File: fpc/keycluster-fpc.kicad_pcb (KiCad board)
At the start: 2 copper layers, 15 x 13.7 mm, 2 parts

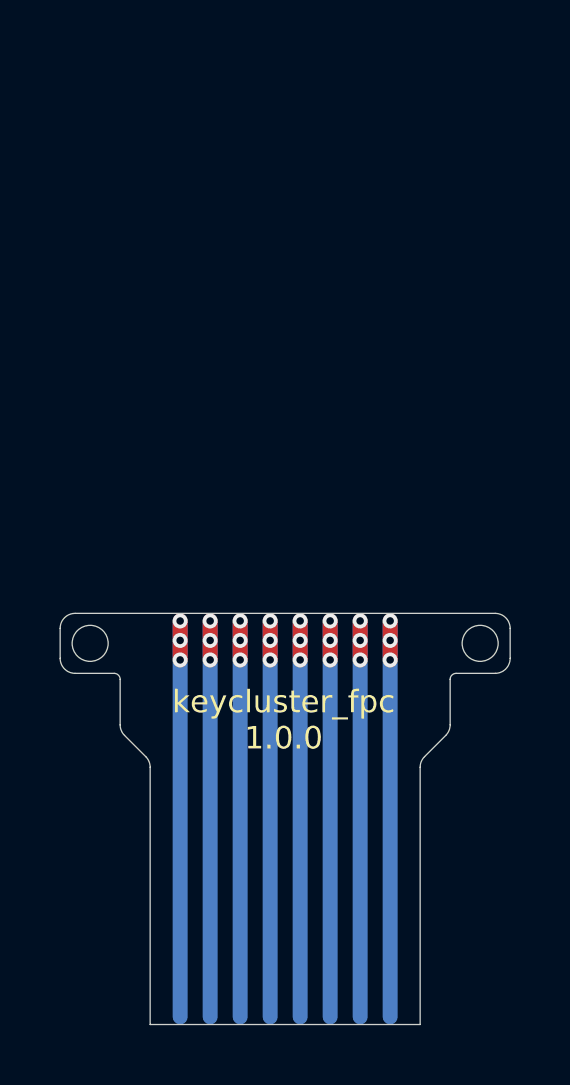
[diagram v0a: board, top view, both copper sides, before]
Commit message: Add incomplete key cluster FPC.
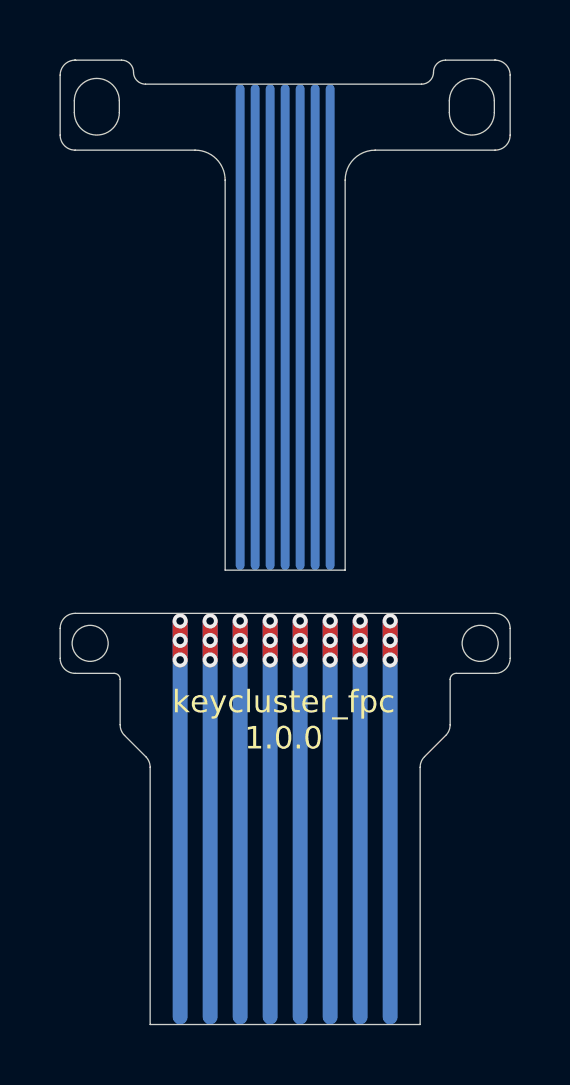
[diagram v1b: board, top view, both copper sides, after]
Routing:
- net (no net): track 116.0 -> 227.2 mm
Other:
- board size 15 x 13.7 mm -> 15 x 32.1 mm
- net class Default: trace_width 0.5 -> 0.3
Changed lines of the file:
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@@
-(kicad_pcb (version 20171130) (host pcbnew 5.1.4-e60b266~84~ubuntu18.04.1)
+(kicad_pcb (version 20171130) (host pcbnew 5.1.5-52549c5~86~ubuntu18.04.1)
   (general
     (thickness 1.6)
-    (drawings 60)
-    (tracks 40)
+    (drawings 91)
+    (tracks 47)
     (zones 0)
     (modules 2)
@@
     (36 B.SilkS user)
     (37 F.SilkS user)
-    (38 B.Mask user hide)
-    (39 F.Mask user hide)
+    (38 B.Mask user)
+    (39 F.Mask user)
     (40 Dwgs.User user)
     (41 Cmts.User user)
@@
   )
   (setup
-    (last_trace_width 0.5)
+    (last_trace_width 0.3)
     (trace_clearance 0)
     (zone_clearance 0.508)
@@
   (net_class Default "This is the default net class."
     (clearance 0)
-    (trace_width 0.5)
+    (trace_width 0.3)
     (via_dia 0.5)
     (via_drill 0.25)
@@
   (gr_arc (start 207.3 136.847262) (end 207.5 136.847257) (angle -89.98075418) (layer Edge.Cuts) (width 0.01))
   (gr_arc (start 218.7 136.847262) (end 218.7 136.647257) (angle -90.00839267) (layer Edge.Cuts) (width 0.01))
+  (gr_arc (start 219.222717 117.565717) (end 219.97271 117.56571) (angle -179.9978282) (layer Edge.Cuts) (width 0.01))
+  (gr_line (start 219.97271 117.56571) (end 219.97271 117.954501) (angle 90) (layer Edge.Cuts) (width 0.01))
+  (gr_arc (start 219.222725 117.95448) (end 218.47271 117.954501) (angle -179.9990721) (layer Edge.Cuts) (width 0.01))
+  (gr_line (start 218.47271 117.954501) (end 218.47271 117.56571) (angle 90) (layer Edge.Cuts) (width 0.01))
+  (gr_arc (start 206.72271 117.565717) (end 207.47271 117.56571) (angle -179.9989939) (layer Edge.Cuts) (width 0.01))
+  (gr_line (start 207.47271 117.56571) (end 207.47271 117.954501) (angle 90) (layer Edge.Cuts) (width 0.01))
+  (gr_arc (start 206.722717 117.95448) (end 205.97271 117.954501) (angle -179.9979064) (layer Edge.Cuts) (width 0.01))
+  (gr_line (start 205.97271 117.954501) (end 205.97271 117.56571) (angle 90) (layer Edge.Cuts) (width 0.01))
+  (gr_line (start 205.5 116.706895) (end 205.5 118.707214) (angle 90) (layer Edge.Cuts) (width 0.01))
+  (gr_line (start 220.5 118.707214) (end 220.5 116.706895) (angle 90) (layer Edge.Cuts) (width 0.01))
+  (gr_line (start 211 120.207214) (end 211 133.207214) (angle 90) (layer Edge.Cuts) (width 0.01))
+  (gr_line (start 215 120.207214) (end 215 133.207214) (angle 90) (layer Edge.Cuts) (width 0.01))
+  (gr_arc (start 205.999992 116.706885) (end 206.017857 116.207214) (angle -92.05235931) (layer Edge.Cuts) (width 0.01))
+  (gr_arc (start 220.000008 116.706885) (end 220.5 116.706895) (angle -92.05528568) (layer Edge.Cuts) (width 0.01))
+  (gr_line (start 205.982143 116.207214) (end 207.54542 116.207214) (angle 90) (layer Edge.Cuts) (width 0.01))
+  (gr_line (start 206 119.207214) (end 210 119.207214) (angle 90) (layer Edge.Cuts) (width 0.01))
+  (gr_line (start 215 133.207214) (end 211 133.207214) (angle 90) (layer Edge.Cuts) (width 0.01))
+  (gr_line (start 211 128.207214) (end 215 128.207214) (angle 90) (layer Cmts.User) (width 0.01))
+  (gr_line (start 216 119.207214) (end 220 119.207214) (angle 90) (layer Edge.Cuts) (width 0.01))
+  (gr_line (start 217.54542 117.007214) (end 208.34542 117.007214) (angle 90) (layer Edge.Cuts) (width 0.01))
+  (gr_arc (start 205.999992 118.707219) (end 205.5 118.707214) (angle -90.0025559) (layer Edge.Cuts) (width 0.01))
+  (gr_arc (start 220.000008 118.707219) (end 220 119.207214) (angle -90.00780572) (layer Edge.Cuts) (width 0.01))
+  (gr_line (start 217.94542 116.607214) (end 217.94542 116.607214) (angle 90) (layer Edge.Cuts) (width 0.01))
+  (gr_line (start 207.94542 116.607214) (end 207.94542 116.607214) (angle 90) (layer Edge.Cuts) (width 0.01))
+  (gr_line (start 218.34542 116.207214) (end 220.017857 116.207214) (angle 90) (layer Edge.Cuts) (width 0.01))
+  (gr_arc (start 217.54542 116.607215) (end 217.54542 117.007214) (angle -89.99932997) (layer Edge.Cuts) (width 0.01))
+  (gr_arc (start 218.345434 116.607226) (end 218.34542 116.207214) (angle -89.98423066) (layer Edge.Cuts) (width 0.01))
+  (gr_arc (start 208.345427 116.607215) (end 207.94542 116.607214) (angle -90.00570683) (layer Edge.Cuts) (width 0.01))
+  (gr_arc (start 207.54542 116.607226) (end 207.94542 116.607214) (angle -89.97978138) (layer Edge.Cuts) (width 0.01))
+  (gr_arc (start 210.000001 120.207211) (end 211 120.207214) (angle -90.00215464) (layer Edge.Cuts) (width 0.01))
+  (gr_arc (start 215.999999 120.207211) (end 216 119.207214) (angle -89.99952954) (layer Edge.Cuts) (width 0.01))
   (segment (start 210.5 134.9) (end 210.5 148.1) (width 0.5) (layer B.Cu) (net 0))
   (segment (start 211.5 134.9) (end 211.5 148.1) (width 0.5) (layer B.Cu) (net 0))
@@
   (segment (start 215.5 136.2) (end 215.5 134.902267) (width 0.5) (layer F.Cu) (net 0))
   (segment (start 216.5 136.2) (end 216.5 134.902267) (width 0.5) (layer F.Cu) (net 0))
+  (segment (start 212.5 133.05) (end 212.5 117.162224) (width 0.3) (layer B.Cu) (net 0))
+  (segment (start 213 133.05) (end 213 117.162224) (width 0.3) (layer B.Cu) (net 0))
+  (segment (start 213.5 133.05) (end 213.5 117.162224) (width 0.3) (layer B.Cu) (net 0))
+  (segment (start 214 133.05) (end 214 117.162224) (width 0.3) (layer B.Cu) (net 0))
+  (segment (start 214.5 133.05) (end 214.5 117.162224) (width 0.3) (layer B.Cu) (net 0))
+  (segment (start 212 133.05) (end 212 117.162224) (width 0.3) (layer B.Cu) (net 0))
+  (segment (start 211.5 133.05) (end 211.5 117.162224) (width 0.3) (layer B.Cu) (net 0))
 )

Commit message: Add holes and soldermask.
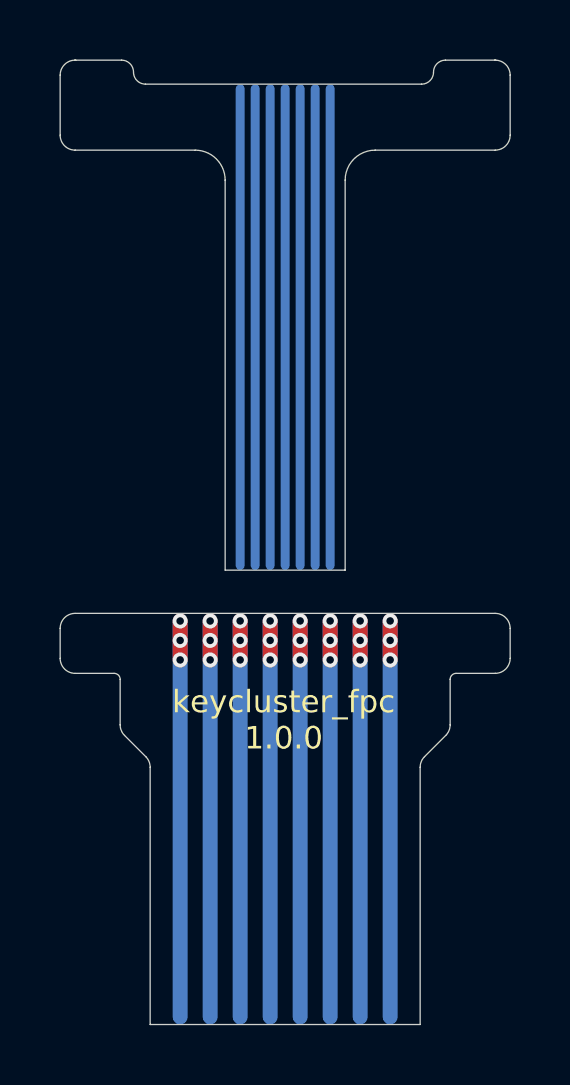
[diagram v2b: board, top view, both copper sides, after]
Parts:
- removed the ? at (219.5, 135.6)
- removed the ? at (206.5, 135.6)
- added ?: , UGL:hole_1.2000000476837158mm, F.Cu at (219.2, 117.8)
- added ?: , UGL:hole_1.2000000476837158mm, F.Cu at (206.7, 117.8)
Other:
- outline, holes or cut-outs redrawn
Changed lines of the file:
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@@
   (general
     (thickness 1.6)
-    (drawings 91)
+    (drawings 83)
     (tracks 47)
     (zones 0)
@@
     (mod_text_size 1 1)
     (mod_text_width 0.15)
-    (pad_size 1.5 1.5)
-    (pad_drill 0.6)
+    (pad_size 1.5 1.89)
+    (pad_drill 1.5)
     (pad_to_mask_clearance 0)
     (aux_axis_origin 0 0)
@@
     (diff_pair_gap 0.25)
   )
-  (module UGL:hole_1.2000000476837158mm locked (layer F.Cu)
-    (at 219.5 135.647263)
+  (module UGL:hole_1.2000000476837158mm (layer F.Cu)
+    (at 219.222717 117.76)
     (attr virtual)
     (fp_text reference "" (at 0 0) (layer F.SilkS)
@@
       (effects (font (size 1.27 1.27) (thickness 0.15)))
     )
-    (pad "" np_thru_hole circle (at 0 0) (size 1.2 1.2) (drill 1.2) (layers *.Cu *.Mask)
+    (pad "" np_thru_hole oval (at 0 0) (size 1.5 1.89) (drill oval 1.5 1.89) (layers *.Cu *.Mask)
       (clearance 0.00001))
   )
-  (module UGL:hole_1.2000000476837158mm locked (layer F.Cu)
-    (at 206.5 135.647263)
+  (module UGL:hole_1.2000000476837158mm (layer F.Cu)
+    (at 206.72271 117.76)
     (attr virtual)
     (fp_text reference "" (at 0 0) (layer F.SilkS)
@@
       (effects (font (size 1.27 1.27) (thickness 0.15)))
     )
-    (pad "" np_thru_hole circle (at 0 0) (size 1.2 1.2) (drill 1.2) (layers *.Cu *.Mask)
+    (pad "" np_thru_hole oval (at 0 0) (size 1.5 1.89) (drill oval 1.5 1.89) (layers *.Cu *.Mask)
       (clearance 0.00001))
   )
@@
   (gr_line (start 217.5 148.35) (end 225 148.35) (layer Dwgs.User) (width 0.15))
   (gr_line (start 217.5 143.35) (end 225 143.35) (layer Dwgs.User) (width 0.15))
-  (gr_line (start 208.5 145.85) (end 217.5 145.85) (layer B.Mask) (width 5))
+  (gr_line (start 210.945067 130.725205) (end 214.945067 130.725205) (layer B.Mask) (width 5))
   (gr_line (start 205.95 136.15) (end 220.05 136.15) (layer B.Mask) (width 3))
   (gr_line (start 205.95 135.65) (end 220.05 135.65) (layer F.Mask) (width 2))
@@
   (gr_arc (start 207.3 136.847262) (end 207.5 136.847257) (angle -89.98075418) (layer Edge.Cuts) (width 0.01))
   (gr_arc (start 218.7 136.847262) (end 218.7 136.647257) (angle -90.00839267) (layer Edge.Cuts) (width 0.01))
-  (gr_arc (start 219.222717 117.565717) (end 219.97271 117.56571) (angle -179.9978282) (layer Edge.Cuts) (width 0.01))
-  (gr_line (start 219.97271 117.56571) (end 219.97271 117.954501) (angle 90) (layer Edge.Cuts) (width 0.01))
-  (gr_arc (start 219.222725 117.95448) (end 218.47271 117.954501) (angle -179.9990721) (layer Edge.Cuts) (width 0.01))
-  (gr_line (start 218.47271 117.954501) (end 218.47271 117.56571) (angle 90) (layer Edge.Cuts) (width 0.01))
-  (gr_arc (start 206.72271 117.565717) (end 207.47271 117.56571) (angle -179.9989939) (layer Edge.Cuts) (width 0.01))
-  (gr_line (start 207.47271 117.56571) (end 207.47271 117.954501) (angle 90) (layer Edge.Cuts) (width 0.01))
-  (gr_arc (start 206.722717 117.95448) (end 205.97271 117.954501) (angle -179.9979064) (layer Edge.Cuts) (width 0.01))
-  (gr_line (start 205.97271 117.954501) (end 205.97271 117.56571) (angle 90) (layer Edge.Cuts) (width 0.01))
   (gr_line (start 205.5 116.706895) (end 205.5 118.707214) (angle 90) (layer Edge.Cuts) (width 0.01))
   (gr_line (start 220.5 118.707214) (end 220.5 116.706895) (angle 90) (layer Edge.Cuts) (width 0.01))

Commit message: Add missing FPC features and close the outline.
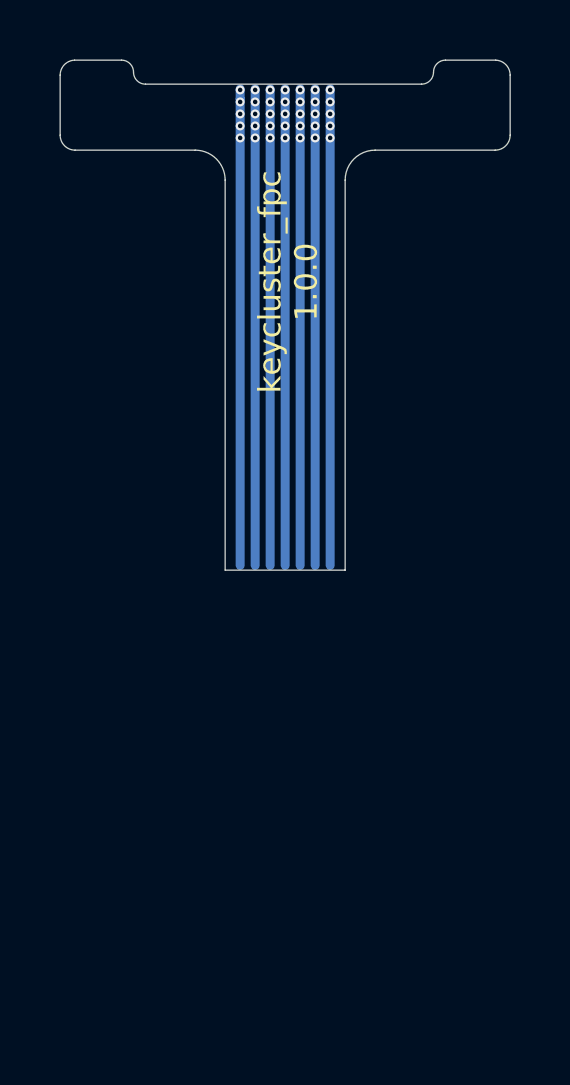
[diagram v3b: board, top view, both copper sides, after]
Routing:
- net (no net): track 227.2 -> 111.2 mm, vias 24 -> 35
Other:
- board size 15 x 32.1 mm -> 15 x 17 mm
- net class Default: via_dia 0.5 -> 0.3; via_drill 0.25 -> 0.15
- rule via_min_drill: 0.25 -> 0.15
- rule via_min_size: 0.25 -> 0.15

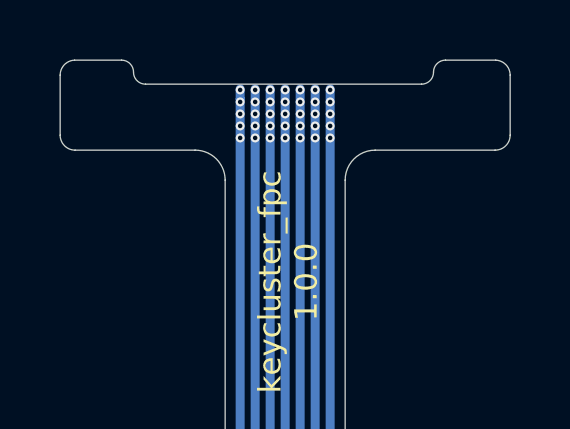
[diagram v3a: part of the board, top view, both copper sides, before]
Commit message: Add top tracks.
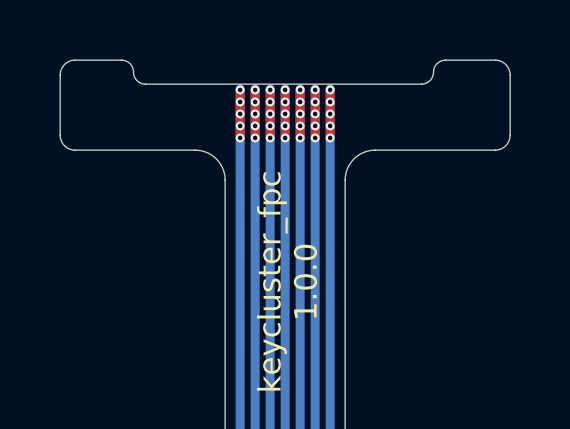
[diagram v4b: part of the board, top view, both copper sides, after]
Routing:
- net (no net): track 111.2 -> 122.4 mm
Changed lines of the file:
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@@
     (thickness 1.6)
     (drawings 43)
-    (tracks 43)
+    (tracks 50)
     (zones 0)
     (modules 2)
@@
   (via (at 214 118.8) (size 0.3) (drill 0.15) (layers F.Cu B.Cu) (net 0))
   (via (at 214.5 118.8) (size 0.3) (drill 0.15) (layers F.Cu B.Cu) (net 0))
+  (segment (start 211.5 117.2) (end 211.5 118.8) (width 0.3) (layer F.Cu) (net 0))
+  (segment (start 212 117.2) (end 212 118.8) (width 0.3) (layer F.Cu) (net 0))
+  (segment (start 212.5 117.2) (end 212.5 118.8) (width 0.3) (layer F.Cu) (net 0))
+  (segment (start 213 117.2) (end 213 118.8) (width 0.3) (layer F.Cu) (net 0))
+  (segment (start 213.5 117.2) (end 213.5 118.8) (width 0.3) (layer F.Cu) (net 0))
+  (segment (start 214 117.2) (end 214 118.8) (width 0.3) (layer F.Cu) (net 0))
+  (segment (start 214.5 117.2) (end 214.5 118.8) (width 0.3) (layer F.Cu) (net 0))
 )

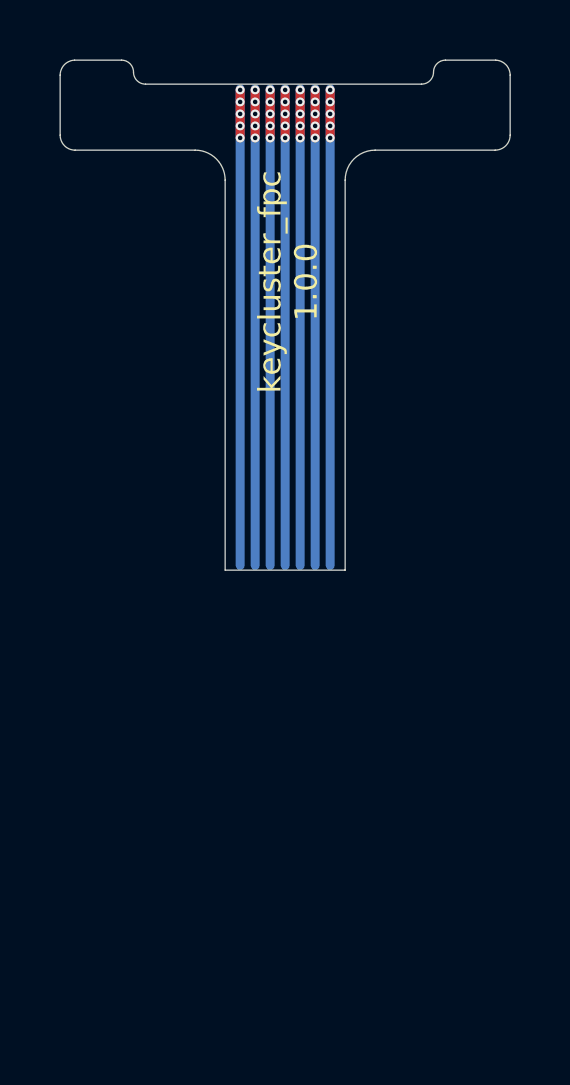
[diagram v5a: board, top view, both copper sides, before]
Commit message: Tweak silk screen positioning.
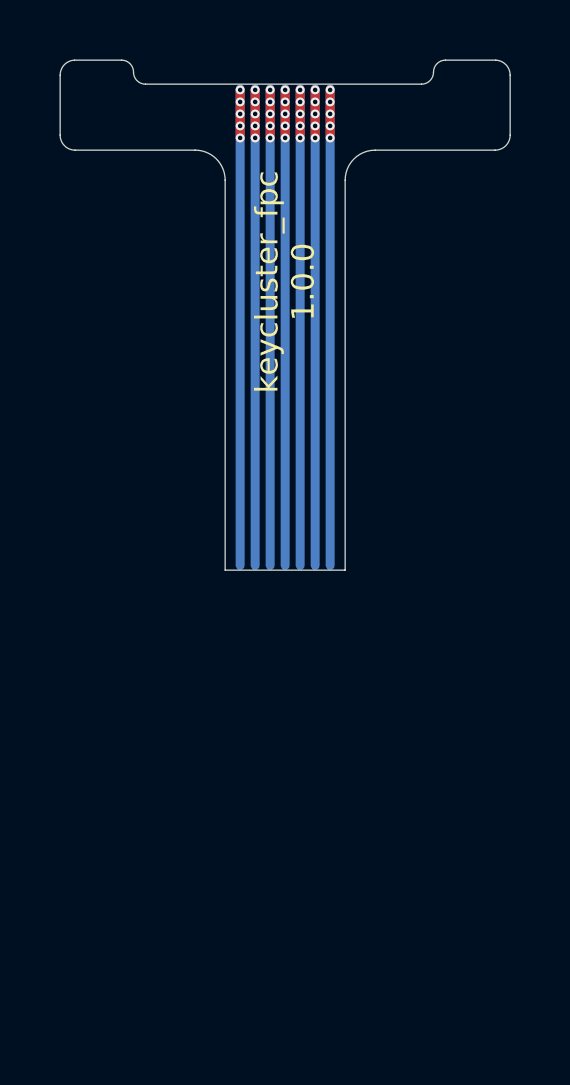
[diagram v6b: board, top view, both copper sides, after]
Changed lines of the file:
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@@
   )
   (gr_line (start 206 117.695524) (end 220 117.695524) (layer B.Mask) (width 3))
-  (gr_text "keycluster_fpc\n1.0.0" (at 213.1 123.6 90) (layer F.SilkS)
+  (gr_text "keycluster_fpc\n1.0.0" (at 213 123.6 90) (layer F.SilkS)
     (effects (font (size 0.75 0.75) (thickness 0.15)))
   )
